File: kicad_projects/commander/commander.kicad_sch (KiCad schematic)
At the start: 10 parts, among them J1 Conn_02x07_Odd_Even, J2 Conn_02x07_Odd_Even, J3 VIK FCC 12, J4 TPS pinout, J5 DS1020-12-6VBT1A-R, J6 PSP 3000 connector SFV4R-4STB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, J7 PSP 2000 raw pins out, U1 Pico, U2 FODM3053

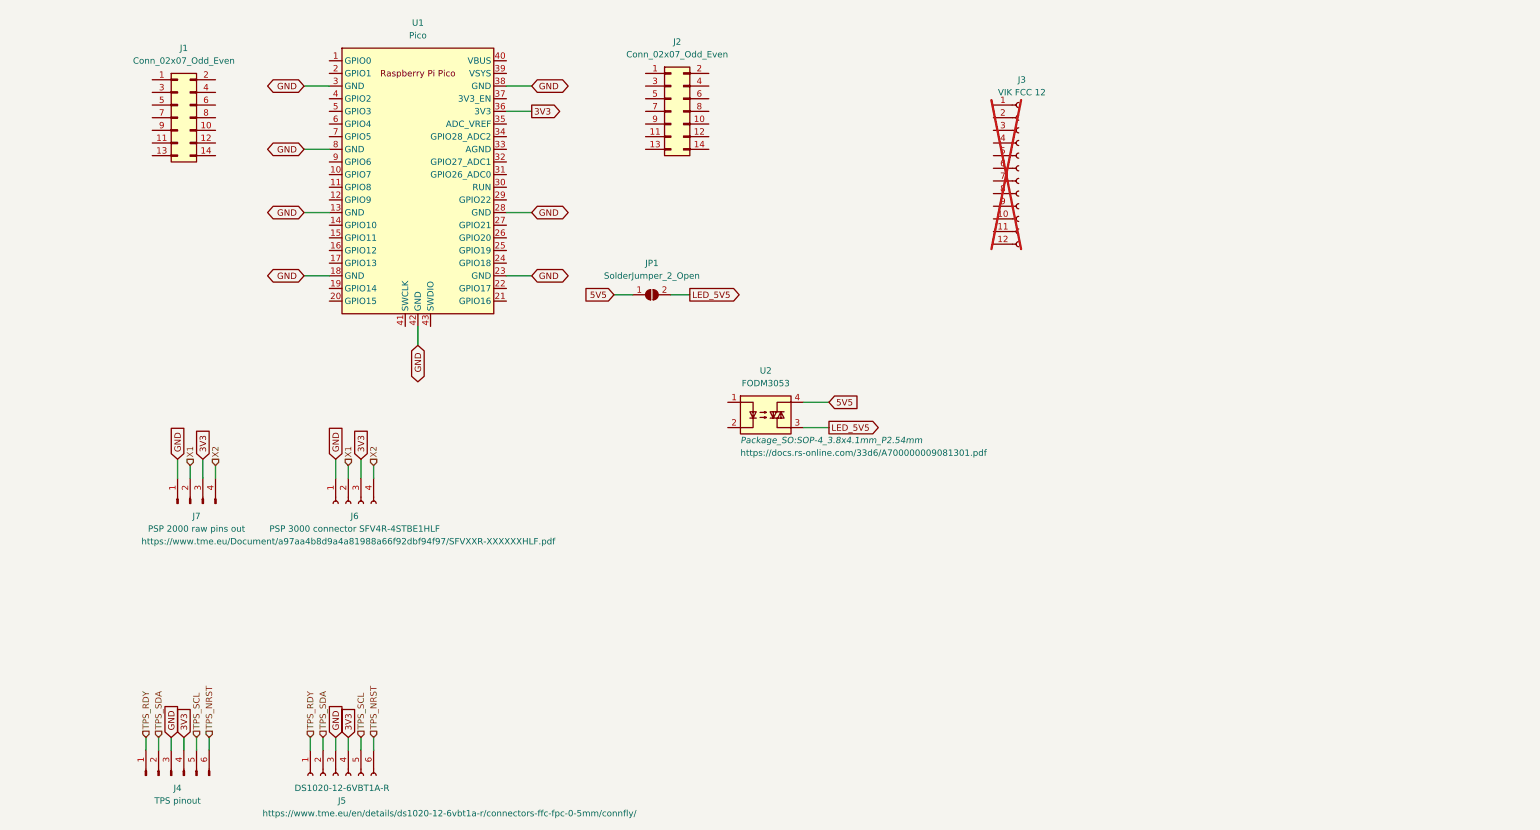
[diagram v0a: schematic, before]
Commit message: Commander board passing DRC
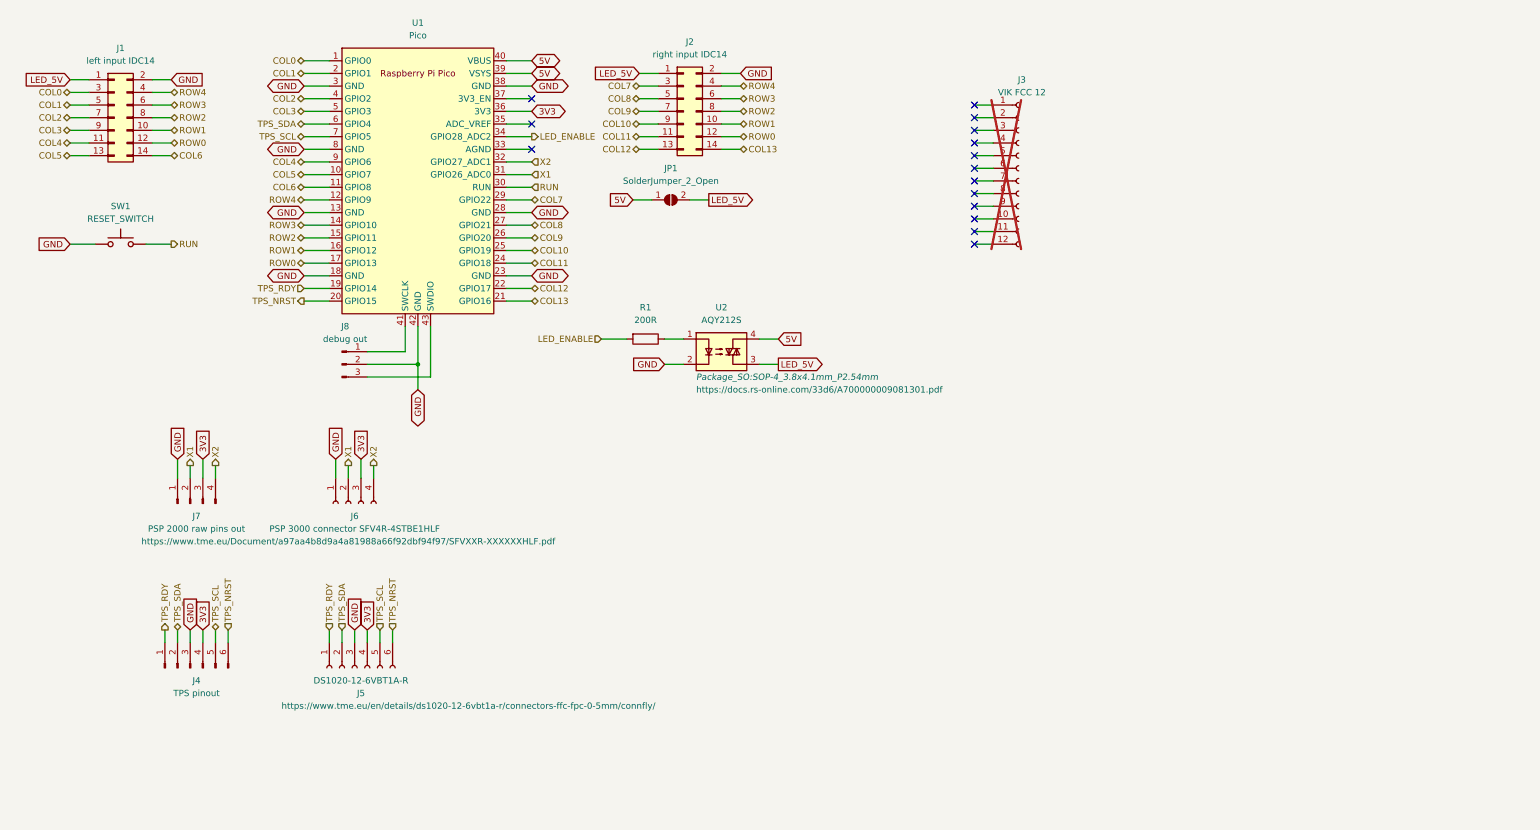
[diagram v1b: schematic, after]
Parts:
- added J8: debug out, Connector_PinHeader_2.54mm:PinHeader_1x03_P2.54mm_Vertical, symbol Connector:Conn_01x03_Pin
- added R1: 200R, Resistor_THT:R_Axial_DIN0207_L6.3mm_D2.5mm_P10.16mm_Horizontal, symbol Device:R
- added SW1: RESET_SWITCH, symbol Switch:SW_Push
- J1: value Conn_02x07_Odd_Even -> left input IDC14
- J2: value Conn_02x07_Odd_Even -> right input IDC14
- U2: value FODM3053 -> AQY212S
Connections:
- net 5V5 is gone; now on net 5V: JP1.1 (A), U2.4
- net LED_5V5 is gone; now on net LED_5V: JP1.2 (B), U2.3
- net GND: now also J1.2 (Pin_2), J2.2 (Pin_2), U2.2, J8.2 (Pin_2), SW1.1
- net TPS_NRST: now also U1.20 (GPIO15)
- net TPS_RDY: now also U1.19 (GPIO14)
- net TPS_SCL: now also U1.7 (GPIO5)
- net TPS_SDA: now also U1.6 (GPIO4)
- net X1: now also U1.31 (GPIO26_ADC0)
- net X2: now also U1.32 (GPIO27_ADC1)
- net COL0: now reaches U1.1 (GPIO0)
- net COL0: now also J1.3 (Pin_3)
- net COL5: now reaches U1.10 (GPIO7)
- net COL5: now also J1.13 (Pin_13)
- net COL6: now reaches U1.11 (GPIO8)
- net COL6: now also J1.14 (Pin_14)
- net ROW4: now reaches U1.12 (GPIO9)
- net ROW4: now also J1.4 (Pin_4), J2.4 (Pin_4)
- net ROW3: now reaches U1.14 (GPIO10)
- net ROW3: now also J1.6 (Pin_6), J2.6 (Pin_6)
- net ROW2: now reaches U1.15 (GPIO11)
- net ROW2: now also J1.8 (Pin_8), J2.8 (Pin_8)
- net ROW1: now reaches U1.16 (GPIO12)
- net ROW1: now also J1.10 (Pin_10), J2.10 (Pin_10)
- net ROW0: now reaches U1.17 (GPIO13)
- net ROW0: now also J1.12 (Pin_12), J2.12 (Pin_12)
- net COL1: now reaches U1.2 (GPIO1)
- net COL1: now also J1.5 (Pin_5)
- net COL13: now reaches U1.21 (GPIO16)
- net COL13: now also J2.14 (Pin_14)
- net COL12: now reaches U1.22 (GPIO17)
- net COL12: now also J2.13 (Pin_13)
- net COL11: now reaches U1.24 (GPIO18)
- net COL11: now also J2.11 (Pin_11)
- net COL10: now reaches U1.25 (GPIO19)
- net COL10: now also J2.9 (Pin_9)
- net COL9: now reaches U1.26 (GPIO20)
- net COL9: now also J2.7 (Pin_7)
- net COL8: now reaches U1.27 (GPIO21)
- net COL8: now also J2.5 (Pin_5)
- net COL7: now reaches U1.29 (GPIO22)
- net COL7: now also J2.3 (Pin_3)
- net RUN: now reaches U1.30 (RUN)
- net RUN: now also SW1.2
- net LED_ENABLE: now reaches U1.34 (GPIO28_ADC2)
- net LED_ENABLE: now also R1.2
- net 5V: now reaches U1.39 (VSYS)
- net 5V: now also U1.40 (VBUS)
- net COL2: now reaches U1.4 (GPIO2)
- net COL2: now also J1.7 (Pin_7)
- net at U1.41 (SWCLK): now also J8.1 (Pin_1)
- net at U1.43 (SWDIO): now also J8.3 (Pin_3)
- net COL3: now reaches U1.5 (GPIO3)
- net COL3: now also J1.9 (Pin_9)
- net COL4: now reaches U1.9 (GPIO6)
- net COL4: now also J1.11 (Pin_11)
- net at U2.1: now also R1.1
- net LED_5V: now reaches J1.1 (Pin_1)
- net LED_5V: now also J2.1 (Pin_1)
- no-connect marks 0 -> 15
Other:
- moved on the sheet: J1, J2, J4, J5, JP1, U2

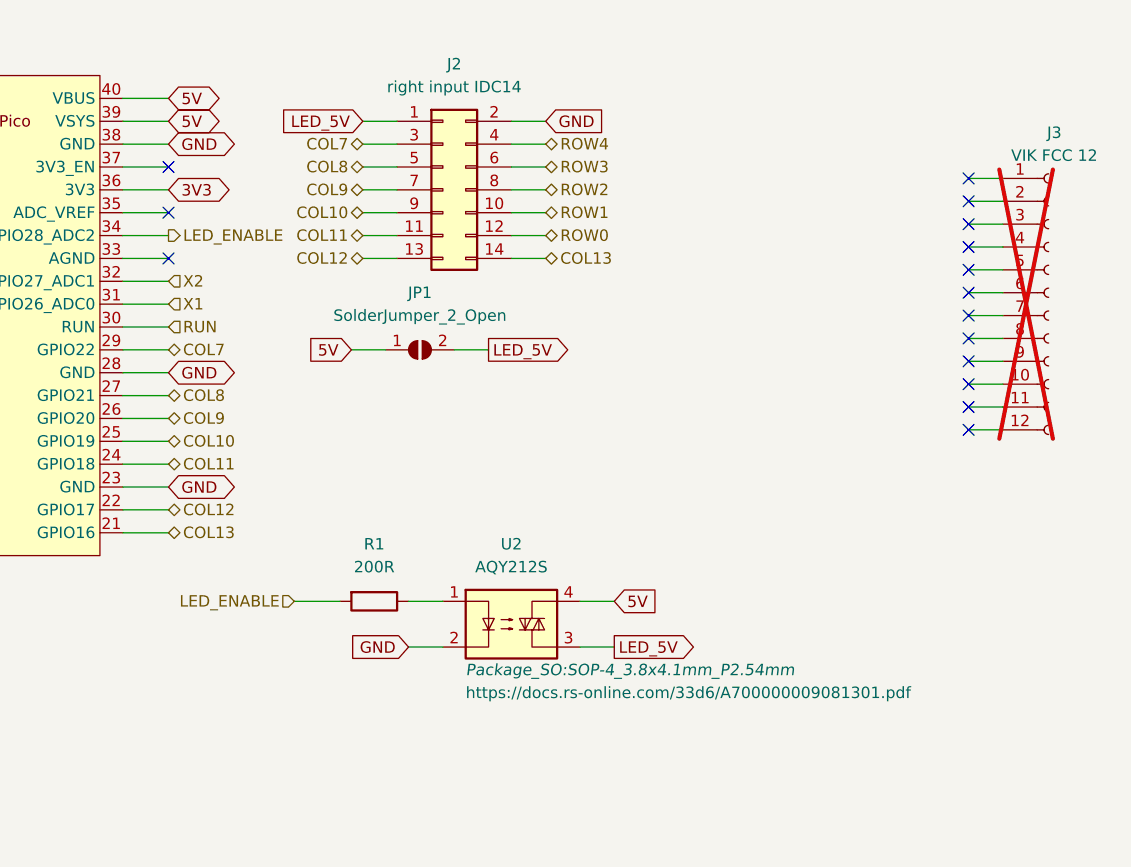
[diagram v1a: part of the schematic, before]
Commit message: Replace a relay with a MOSFET (like a pro)
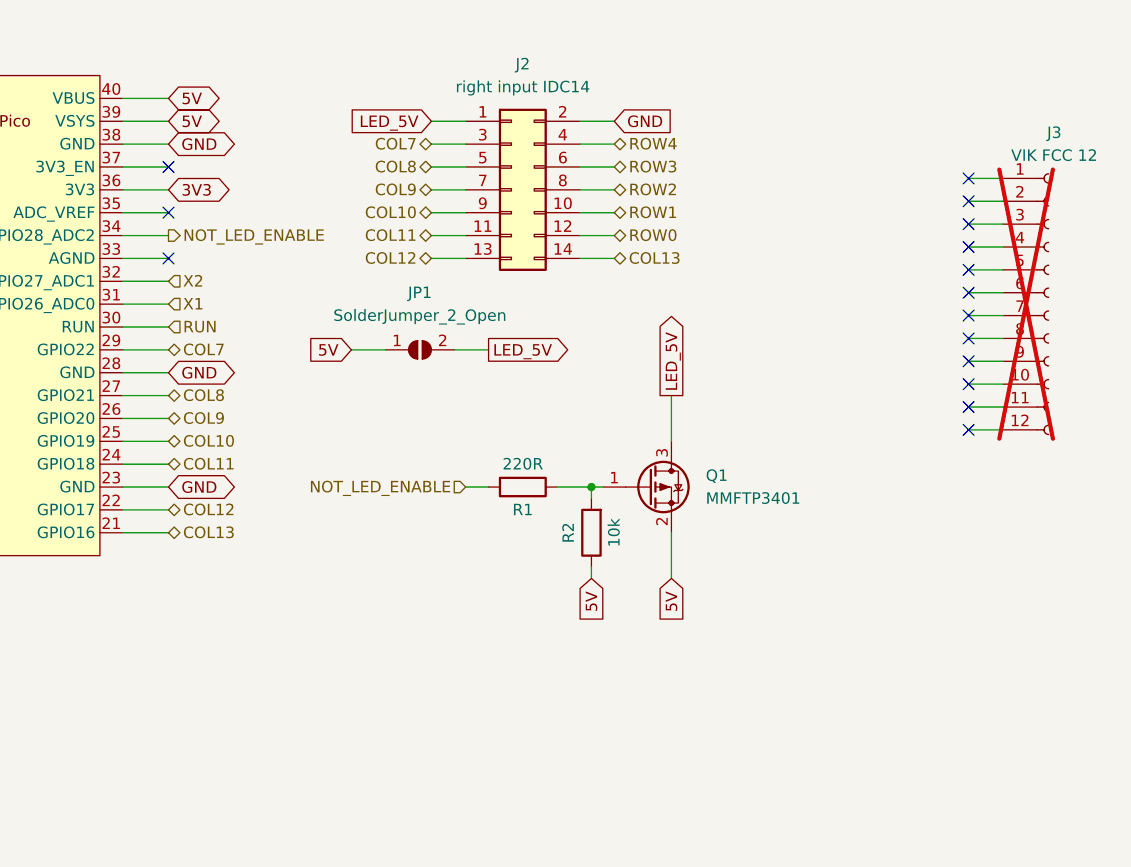
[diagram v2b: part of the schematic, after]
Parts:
- removed U2: AQY212S, Package_SO:SOP-4_3.8x4.1mm_P2.54mm, symbol Relay_SolidState:FODM3053
- added Q1: MMFTP3401, Package_TO_SOT_SMD:SOT-23, symbol Transistor_FET:AO3401A
- added R2: 10k, Resistor_SMD:R_0805_2012Metric_Pad1.20x1.40mm_HandSolder, symbol Device:R
- R1: value 200R -> 220R; footprint Resistor_THT:R_Axial_DIN0207_L6.3mm_D2.5mm_P10.16mm_Horizontal -> Resistor_SMD:R_0805_2012Metric_Pad1.20x1.40mm_HandSolder; expected power 100mW -> (none)
- SW1: footprint (none) -> Button_Switch_THT:SW_PUSH_6mm_H4.3mm
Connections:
- net 5V: now also Q1.2 (S), R2.1
- net LED_5V: now also Q1.3 (D)
- net at R1.1: now also Q1.1 (G), R2.2
- net LED_ENABLE renamed NOT_LED_ENABLE
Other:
- moved on the sheet: J2

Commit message: big commander WIP
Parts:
- added SW2, SW3, SW4: SW_Push, revolt_footprints:SW_PG1350_reversible_with_keycap_outline, symbol Switch:SW_Push
- J1: value left input IDC14 -> right input IDC14
- J2: value right input IDC14 -> left input IDC14
- J4, J5, J6, J7: now not fitted; now left out of the parts list
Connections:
- net TPS_NRST: no longer U1.20 (GPIO15)
- net TPS_RDY: no longer U1.19 (GPIO14)
- net TPS_SCL: no longer U1.7 (GPIO5)
- net TPS_SDA: no longer U1.6 (GPIO4)
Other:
- moved on the sheet: J1, J2, J8

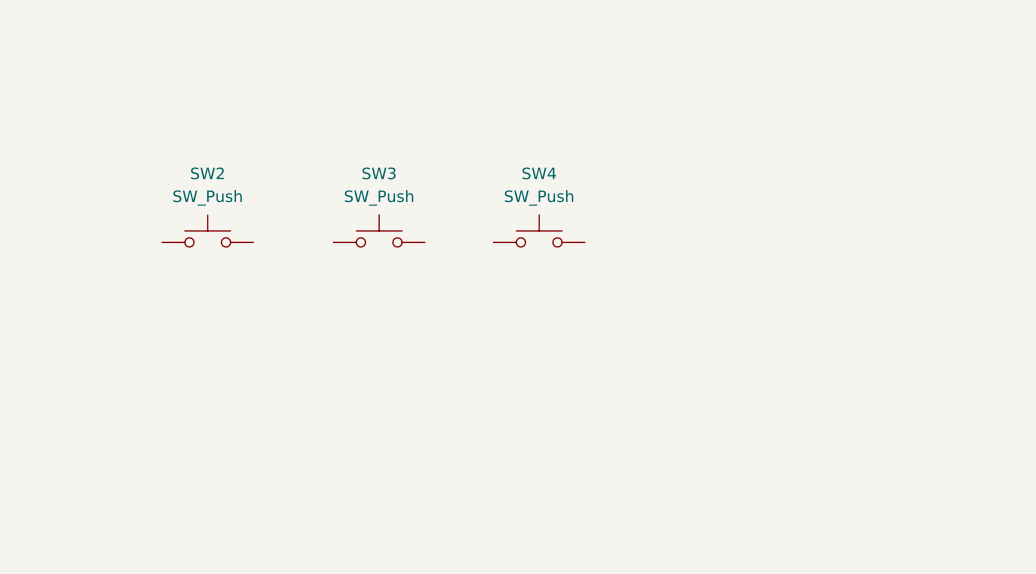
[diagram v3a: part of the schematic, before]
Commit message: trackpoint socket footprints
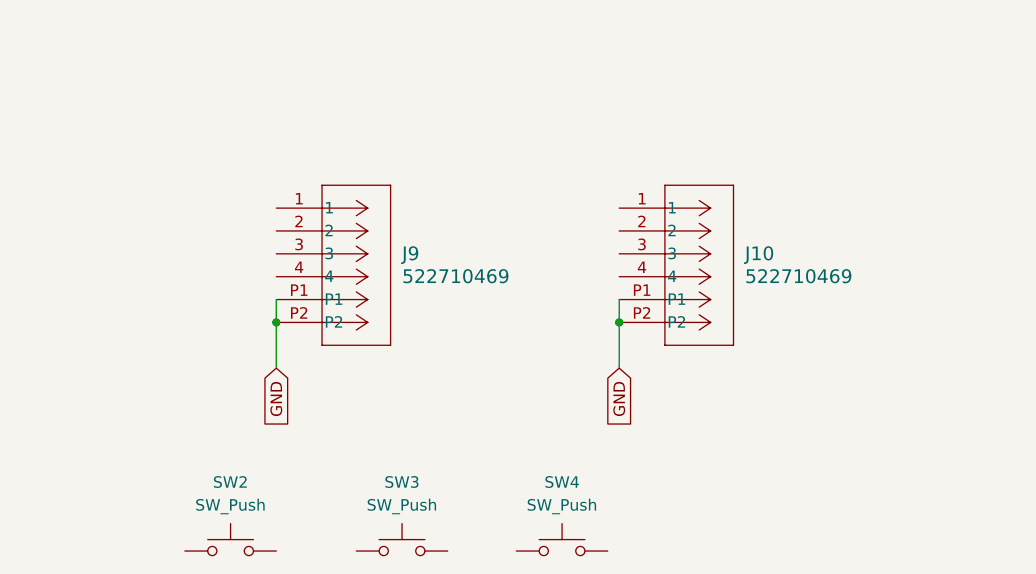
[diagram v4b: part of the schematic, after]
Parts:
- added J10, J9: 522710469, revolt_footprints:CON_522710469_MOL, symbol revolt_symbols:522710469
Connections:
- net GND: now also J10.P1, J10.P2, J9.P1, J9.P2
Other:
- moved on the sheet: SW2, SW3, SW4

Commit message: commander board rev2, pre-manufacture
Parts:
- removed J10: 522710469, revolt_footprints:CON_522710469_MOL, symbol revolt_symbols:522710469
- added J10, J11, J12, J13: Conn_02x01, Connector_PinHeader_2.54mm:PinHeader_2x01_P2.54mm_Vertical, symbol Connector_Generic:Conn_02x01
- added JP2, JP3, JP4, JP5: SolderJumper_2_Bridged, Jumper:SolderJumper-2_P1.3mm_Bridged2Bar_RoundedPad1.0x1.5mm, symbol Jumper:SolderJumper_2_Bridged
- added Q2: NPN - MMBT2222A, Package_TO_SOT_SMD:SOT-23, symbol Device:Q_NPN_BEC
- J9: footprint revolt_footprints:CON_522710469_MOL -> revolt_footprints:HC-FPC-05-09-4RLTAG; LCSC (none) -> C5213746
- JP1: now left out of the parts list
- Q1: value MMFTP3401 -> AO3401A; LCSC (none) -> C15127
- R1: value 220R -> 1k; LCSC (none) -> C17513
- R2: LCSC (none) -> C17414
- SW2, SW3, SW4: footprint revolt_footprints:SW_PG1350_reversible_with_keycap_outline -> keyswitches:Kailh_socket_PG1350_optional
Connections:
- net 3V3: now also J12.1 (Pin_1), JP4.1 (A)
- net 5V: now also R2.2; no longer R2.1
- net GND: now also J9.5 (P1), J9.6 (P2), SW2.2, SW3.2, SW4.2, J10.1 (Pin_1), JP2.1 (A), Q2.2 (E); no longer J9.P1, J9.P2
- net X1: now also J11.1 (Pin_1), JP3.1 (A)
- net X2: now also J13.1 (Pin_1), JP5.1 (A)
- net LMB: now reaches U1.19 (GPIO14)
- net LMB: now also SW2.1
- net MMB: now reaches U1.20 (GPIO15)
- net MMB: now also SW3.1
- net RMB: now reaches U1.6 (GPIO4)
- net RMB: now also SW4.1
- net at J9.1: now also J10.2 (Pin_2), JP2.2 (B)
- net at J9.2: now also J11.2 (Pin_2), JP3.2 (B)
- net at J9.3: now also J12.2 (Pin_2), JP4.2 (B)
- net at J9.4: now also J13.2 (Pin_2), JP5.2 (B)
- net NOT_LED_ENABLE renamed LED_ENABLE
- new net: Q1.1 (G), Q2.3 (C), R2.1
- new net: Q2.1 (B), R1.1
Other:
- note added: "https://tinyurl.com/238afudx"
- moved on the sheet: J9, JP1, Q1, R1, R2

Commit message: commander rev2 production files
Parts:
- J9: value 522710469 -> HC-FPC-05-09-4RLTAG
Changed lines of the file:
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@@
 			)
 		)
-		(property "Value" "522710469"
+		(property "Value" "HC-FPC-05-09-4RLTAG"
 			(at 165.1 132.0799 0)
 			(effects
@@
 			)
 		)
-		(property "Datasheet" "522710469"
+		(property "Datasheet" "HC-FPC-05-09-4RLTAG"
 			(at 151.13 116.078 0)
 			(effects
